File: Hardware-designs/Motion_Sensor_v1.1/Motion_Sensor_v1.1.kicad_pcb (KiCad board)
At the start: 2 copper layers, 57 x 57 mm, 37 parts, among them J1 UART, J2 Bat, J3 USB_C, J4 I2C, J5 I2C, Q1 AO3407A, SW2 PTS526 SM15 SMTR2 LFS, U1 ESP32-WROOM-32, U2 TP4057, U4 MCP1700

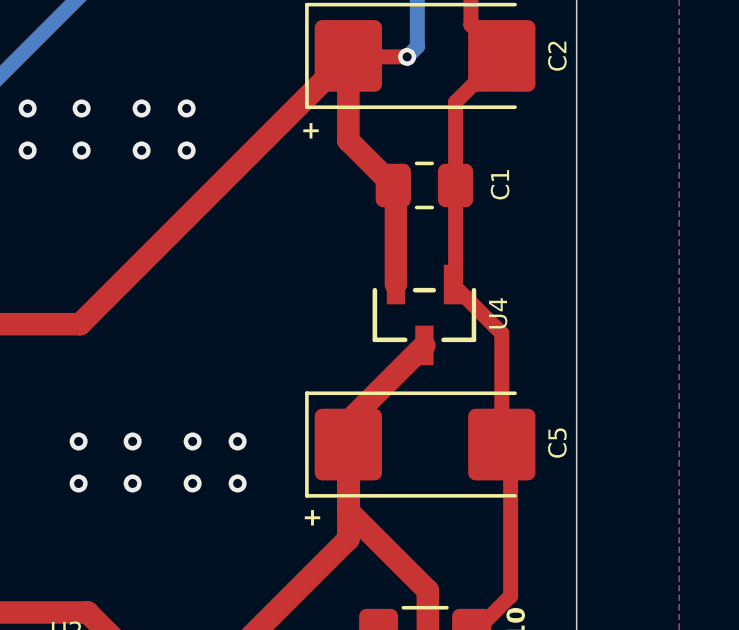
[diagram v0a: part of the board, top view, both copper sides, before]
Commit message: correction voltage regulator
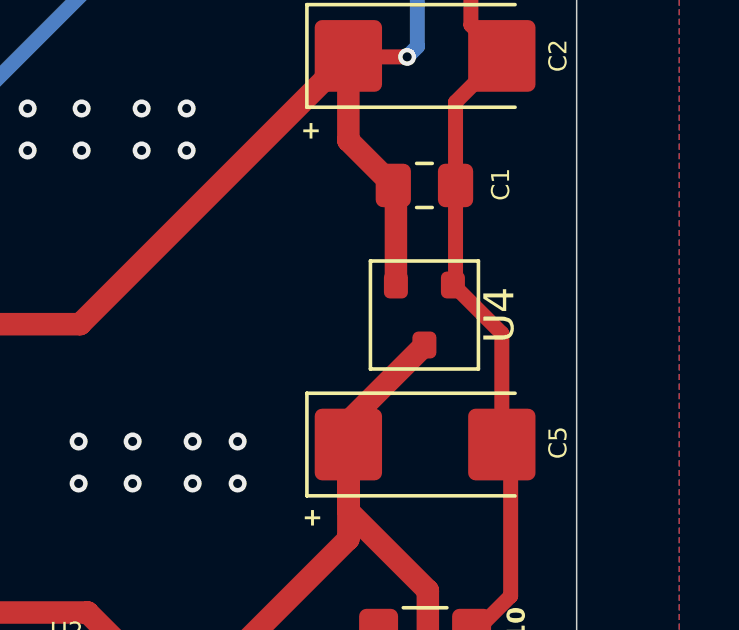
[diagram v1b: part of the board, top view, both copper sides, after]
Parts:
- U4: footprint MCP1700T_3302E_TT 3:SOT-23_MC_MCH -> PCM_Package_TO_SOT_SMD_AKL:SOT-23
- turned U4 to -90 degrees

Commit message: Magnetic Sensor
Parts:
- R14: value 300 -> 300k
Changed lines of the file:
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@@
 			)
 		)
-		(property "Value" "300"
+		(property "Value" "300k"
 			(at 0 1.83 0)
 			(layer "F.Fab")
@@
 		)
 		(embedded_fonts no)
+		(model "/Users/gmixich/OneDrive/github/HueMix-Link-V3/Hardware-designs/Motion_Sensor_v1.1/components/PTS526_SM15_SMTR2_LFS/PTS526SK15SMTR2_LFS.stp"
+			(offset
+				(xyz 0 0 0)
+			)
+			(scale
+				(xyz 1 1 1)
+			)
+			(rotate
+				(xyz 0 0 0)
+			)
+		)
 	)
 	(gr_line

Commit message: Minor KiCad files update for all devices
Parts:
- C3: value 1nF -> 68nF
- R7: value 68k -> 75k
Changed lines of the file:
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@@
 			)
 		)
-		(property "Value" "1nF"
+		(property "Value" "68nF"
 			(at 0 1.68 90)
 			(layer "F.Fab")
@@
 			)
 		)
-		(property "Value" "68k"
+		(property "Value" "75k"
 			(at 0 1.83 90)
 			(layer "F.Fab")
